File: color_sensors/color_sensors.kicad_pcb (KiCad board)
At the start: 2 copper layers, 30 x 22 mm, 10 parts, among them Q1 TEPT4400, Q2 TEPT4400, U1 LM358

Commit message: Make STEP for Color Sensor PCB; remove ultrasonic PCB
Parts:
- R1, R2, R3, R4: footprint IDP_library_0207_5V -> IDP:IDP_library_0207_5V
- SV1: footprint IDP_library_FE04-1 -> IDP:IDP_library_FE04-1
- U1: footprint IDP_library_DIP08 -> IDP:IDP_library_DIP08

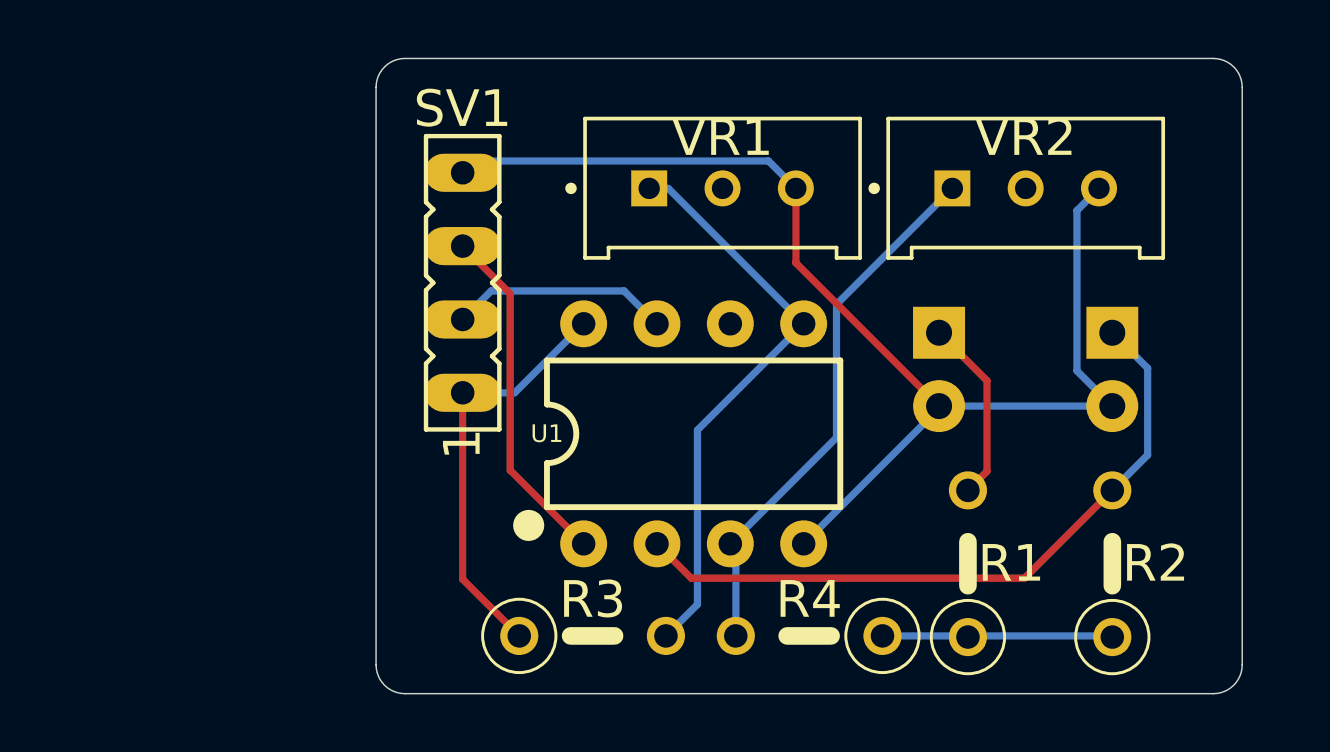
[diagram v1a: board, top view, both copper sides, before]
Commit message: Add mounting holes to Color Sensor PCB
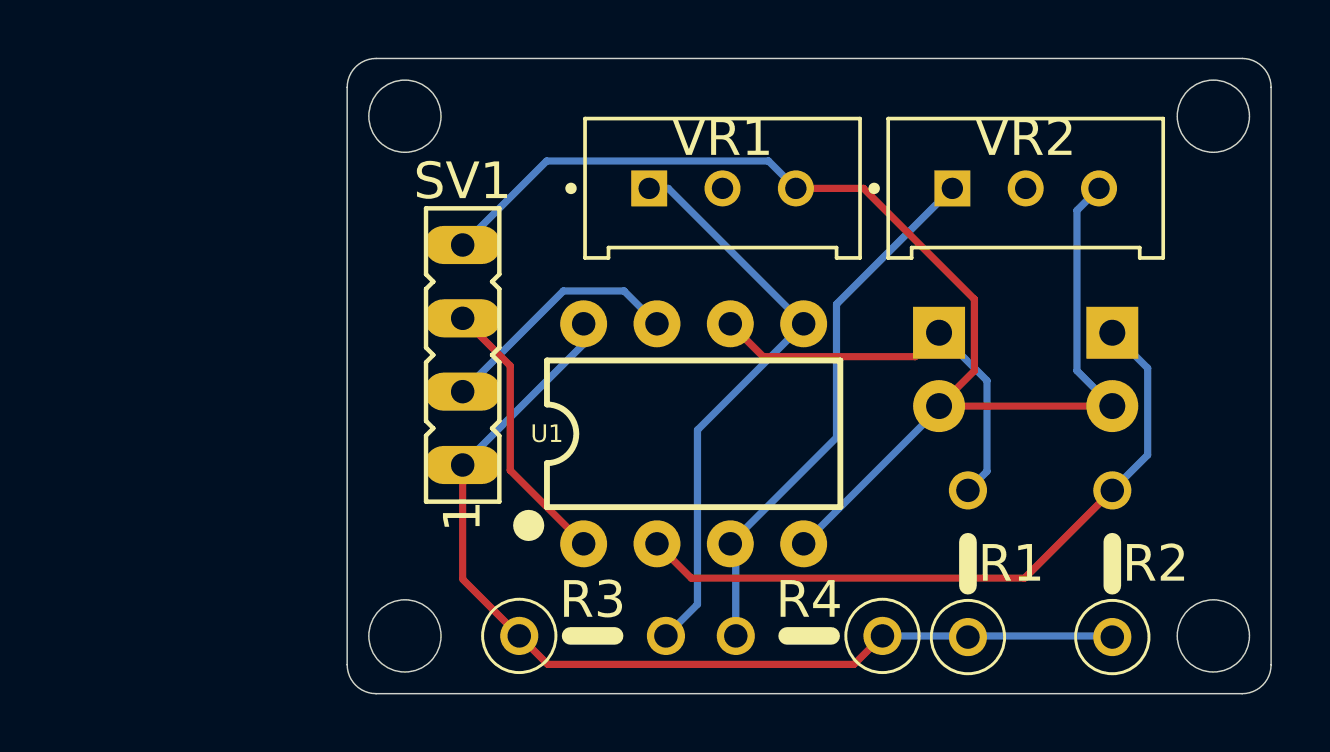
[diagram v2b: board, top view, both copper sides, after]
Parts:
- moved SV1 2.50 mm to (123.0, 148.0)
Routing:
- net +5V: track 22.4 -> 34.7 mm
- net Net-(Q1-Pad1): track 6.42 -> 14.5 mm
- net GND: track 42.8 -> 46.2 mm
- net /green: track 12.0 -> 9.55 mm
- net /red: track 7.61 -> 8.65 mm
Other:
- board size 30 x 22 mm -> 32 x 22 mm

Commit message: Specify resistors; neaten silkscreen; improve 3D model
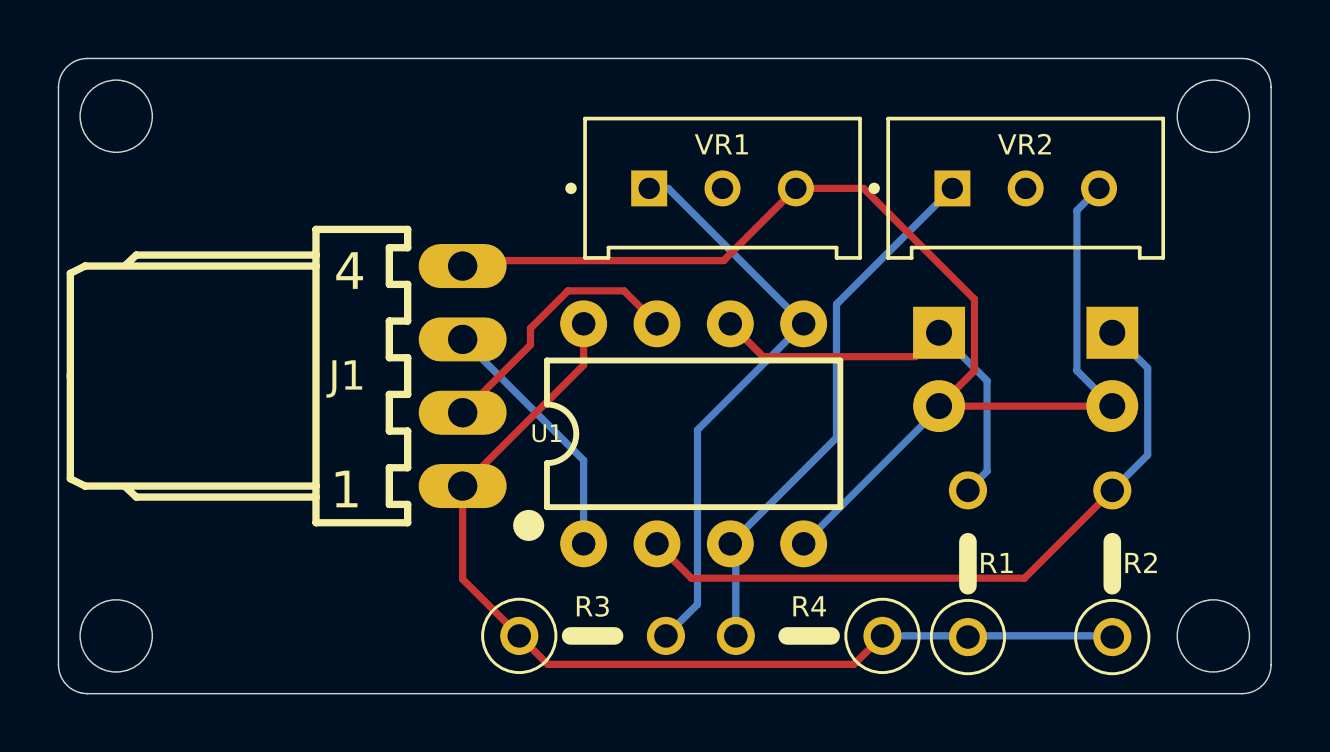
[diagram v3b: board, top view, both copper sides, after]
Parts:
- removed SV1: FE04-1, IDP:IDP_library_FE04-1
- added J1: 22-05-7048-04, IDP:IDP_library_7395-04, F.Cu at (123.0, 150.0)
- R1, R2: value R-EU_0207_5V -> 27k; footprint IDP:IDP_library_0207_5V -> IDP_library_0207_5V
- R3, R4: value R-EU_0207_5V -> 6.8k; footprint IDP:IDP_library_0207_5V -> IDP_library_0207_5V
- U1: footprint IDP:IDP_library_DIP08 -> IDP_library_DIP08
- VR1, VR2: value POT -> 20k
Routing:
- net /green: track 9.55 -> 8.82 mm
- net /red: track 8.65 -> 9.28 mm
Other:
- board size 32 x 22 mm -> 42 x 22 mm
